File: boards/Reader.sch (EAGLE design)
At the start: 46 parts, among them IC1 PIC18F4550_40, T1 BC547, T2 BC547, T3 BC547, X3 PN61729-S

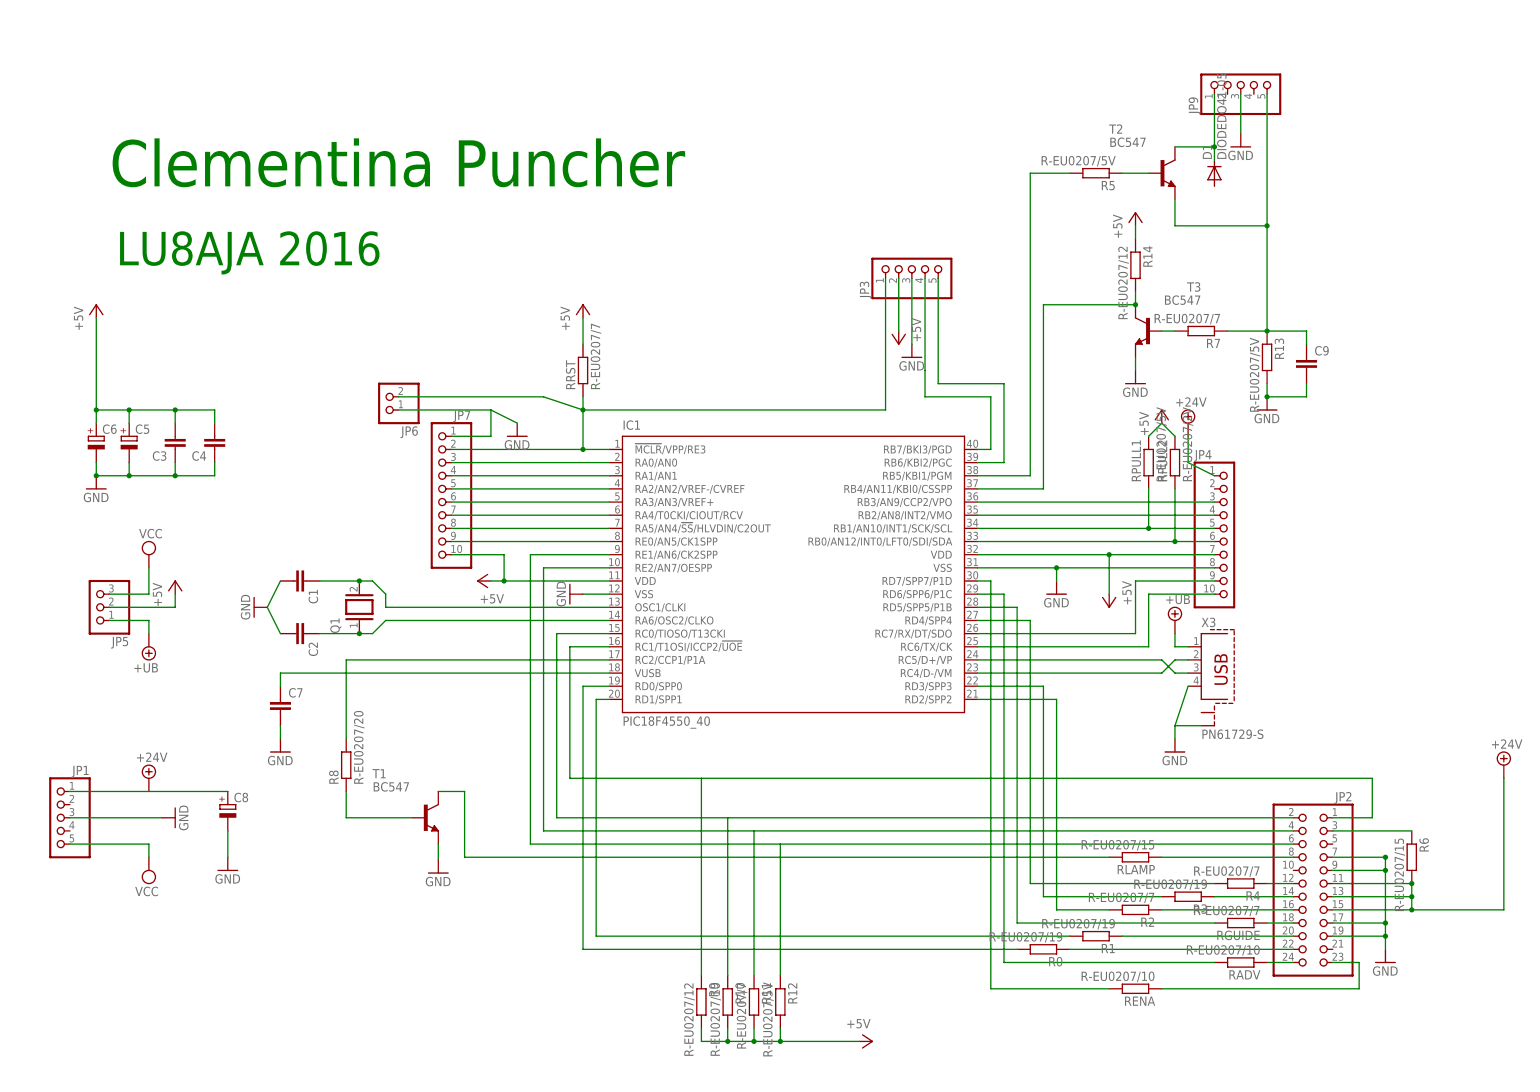
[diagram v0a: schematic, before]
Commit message: Reader: Added new service
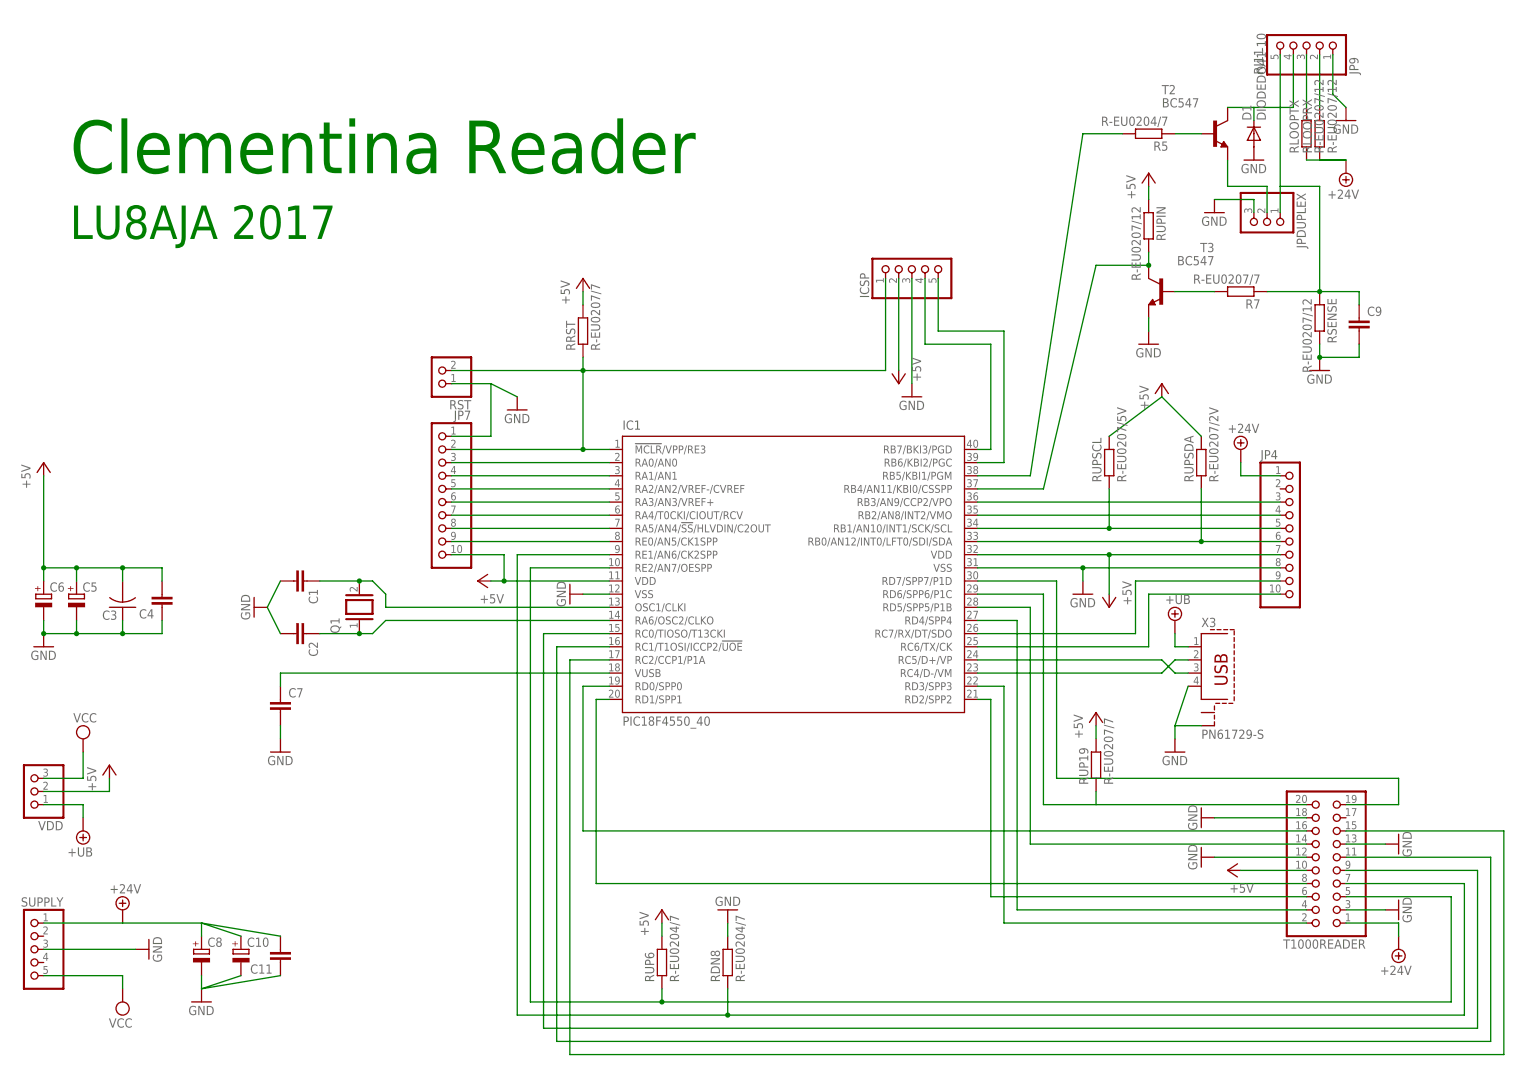
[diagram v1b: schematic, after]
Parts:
- removed JP1: (no value), pinhead:PINHD-1X5
- removed JP2: (no value), pinhead:PINHD-2X12
- removed JP5: (no value), pinhead:PINHD-1X3
- removed JP6: (no value), pinhead:PINHD-1X2
- removed R0, R1, R3: R-EU0207/19, custom:R-EU0207/19
- removed R10, RADV, RENA: R-EU0207/10, custom:R-EU0207/10
- removed R11, R2, R4, RGUIDE: R-EU0207/7, custom:R-EU0207/7
- removed R12, R13, RPULL1: R-EU0207/5V, custom:R-EU0207/5V
- removed R14, R9: R-EU0207/12, custom:R-EU0207/12
- removed R6, RLAMP: R-EU0207/15, custom:R-EU0207/15
- removed R8: R-EU0207/20, custom:R-EU0207/20
- removed RPULL2: R-EU0207/2V, custom:R-EU0207/2V
- removed T1: BC547, transistor:BC547
- added C10: (no value), custom:CPOL-EUE5-8.5
- added C11: (no value), custom:C-EU025-030X050
- added JPDUPLEX, VDD: (no value), pinhead:PINHD-1X3
- added RDN8, RUP6: R-EU0204/7, custom:R-EU0204/7
- added RLOOPRX, RLOOPTX, RSENSE, RUPIN: R-EU0207/12, custom:R-EU0207/12
- added RST: (no value), pinhead:PINHD-1X2
- added RUP19: R-EU0207/7, custom:R-EU0207/7
- added RUPSCL: R-EU0207/5V, custom:R-EU0207/5V
- added RUPSDA: R-EU0207/2V, custom:R-EU0207/2V
- added SUPPLY: (no value), pinhead:PINHD-1X5
- added T1000READER: (no value), pinhead:PINHD-2X10
- C3: device rcl:C-EU050-025X075 -> custom:C-US025-024X044
- C5: device rcl:CPOL-EUE5-8.5 -> custom:CPOL-EUE2.5-6
- C9: device custom:C-EU050-025X075 -> custom:C-EU050-024X044
- D1: value DIODEDO41-05 -> DIODEDO41-10; device custom:DIODEDO41-05 -> custom:DIODEDO41-10
- JP9: value (none) -> RJ11
- R5: value R-EU0207/5V -> R-EU0204/7; device custom:R-EU0207/5V -> custom:R-EU0204/7
- renumbered JP3 to ICSP
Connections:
- removed net N$16: JP2.22, R0.1
- removed net N$33: IC1.RD2/SPP2, R2.2
- removed net N$36: IC1.RD0/SPP0, R0.2
- removed net N$41: JP2.8, RLAMP.1
- removed net N$42: JP2.3, R6.1
- removed net N$43: RLAMP.2, T1.C
- removed net N$44: R8.1, T1.B
- removed net N$7: IC1.RE2/AN7/OESPP, JP2.4, R11.1
- removed net N$8: IC1.RE1/AN6/CK2SPP, JP2.6, R12.1
- net +24V: now also C10.+, C11.2, RLOOPRX.1, RLOOPTX.1, SUPPLY.1, T1000READER.1; no longer JP1.1, JP2.11, JP2.13, JP2.15, R6.2
- net +5V: now also RUP19.2, RUP6.2, RUPIN.1, RUPSCL.2, RUPSDA.2, T1000READER.10, VDD.2; no longer JP5.2, R10.2, R11.2, R12.2, R14.1, R9.2, RPULL1.2, RPULL2.2
- net +UB: now also VDD.1; no longer JP5.1
- net GND: now also C10.-, C11.1, D1.A, JP9.1, JPDUPLEX.3, RDN8.2, RSENSE.2, RST.1, SUPPLY.3, T1000READER.12, T1000READER.13, T1000READER.18, T1000READER.3; no longer JP1.3, JP2.17, JP2.19, JP2.7, JP2.9, JP6.1, JP9.3, R13.2, T1.E
- net N$1: now also IC1.RD2/SPP2, T1000READER.6; no longer JP2.24, RADV.1
- net N$17: now also JP9.3, RLOOPTX.2; no longer IC1.RD3/SPP3, R3.2
- net N$18: now also JPDUPLEX.2, T2.E; no longer JP2.20, R1.1
- net N$19: now also JP9.2, RLOOPRX.2; no longer JP2.18, RGUIDE.1
- net N$20: now also IC1.RD4/SPP4, T1000READER.4; no longer JP2.16, R2.1
- net N$21: now also IC1.RD3/SPP3, T1000READER.2; no longer JP2.14, R3.1
- net N$22: now also IC1.RC2/CCP1/P1A, T1000READER.15; no longer JP2.12, R4.1
- net N$23: now also IC1.RC1/T1OSI/ICCP2/!UOE, T1000READER.11; no longer JP2.23, RENA.1
- net N$24: now also T1000READER.19; no longer RENA.2
- net N$25: now also RUP19.1, T1000READER.20; no longer RADV.2
- net N$26: now also T1000READER.14; no longer RGUIDE.2
- net N$3: now also RST.2; no longer JP6.2
- net N$31: now also RUPSDA.1; no longer RPULL2.1
- net N$32: now also IC1.RD0/SPP0, T1000READER.16; no longer IC1.RD4/SPP4, R4.2
- net N$35: now also T1000READER.8; no longer R1.2
- net N$39: now also RUPSCL.1; no longer RPULL1.1
- net N$4: now also IC1.RC0/TIOSO/T13CKI, T1000READER.9; no longer IC1.RC2/CCP1/P1A, R8.2
- net N$47: now also RUPIN.2; no longer R14.2
- net N$5: now also IC1.RE2/AN7/OESPP, RUP6.1, T1000READER.5; no longer IC1.RC1/T1OSI/ICCP2/!UOE, JP2.1, R9.1
- net N$50: now also JP9.4; no longer JP9.1
- net N$56: now also JPDUPLEX.1, RSENSE.1; no longer R13.1, T2.E
- net N$6: now also IC1.RE1/AN6/CK2SPP, RDN8.1, T1000READER.7; no longer IC1.RC0/TIOSO/T13CKI, JP2.2, R10.1
- net VCC: now also SUPPLY.5, VDD.3; no longer JP1.5, JP5.3
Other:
- note added: "Clementina Reader"
- note added: "LU8AJA 2017"
- note removed: "Clementina Puncher"
- note removed: "LU8AJA 2016"
- moved on the sheet: C3, C4, C5, C6, C8, C9, D1, JP4, JP9, R5, R7, RRST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
